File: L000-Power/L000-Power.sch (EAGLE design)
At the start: 20 parts

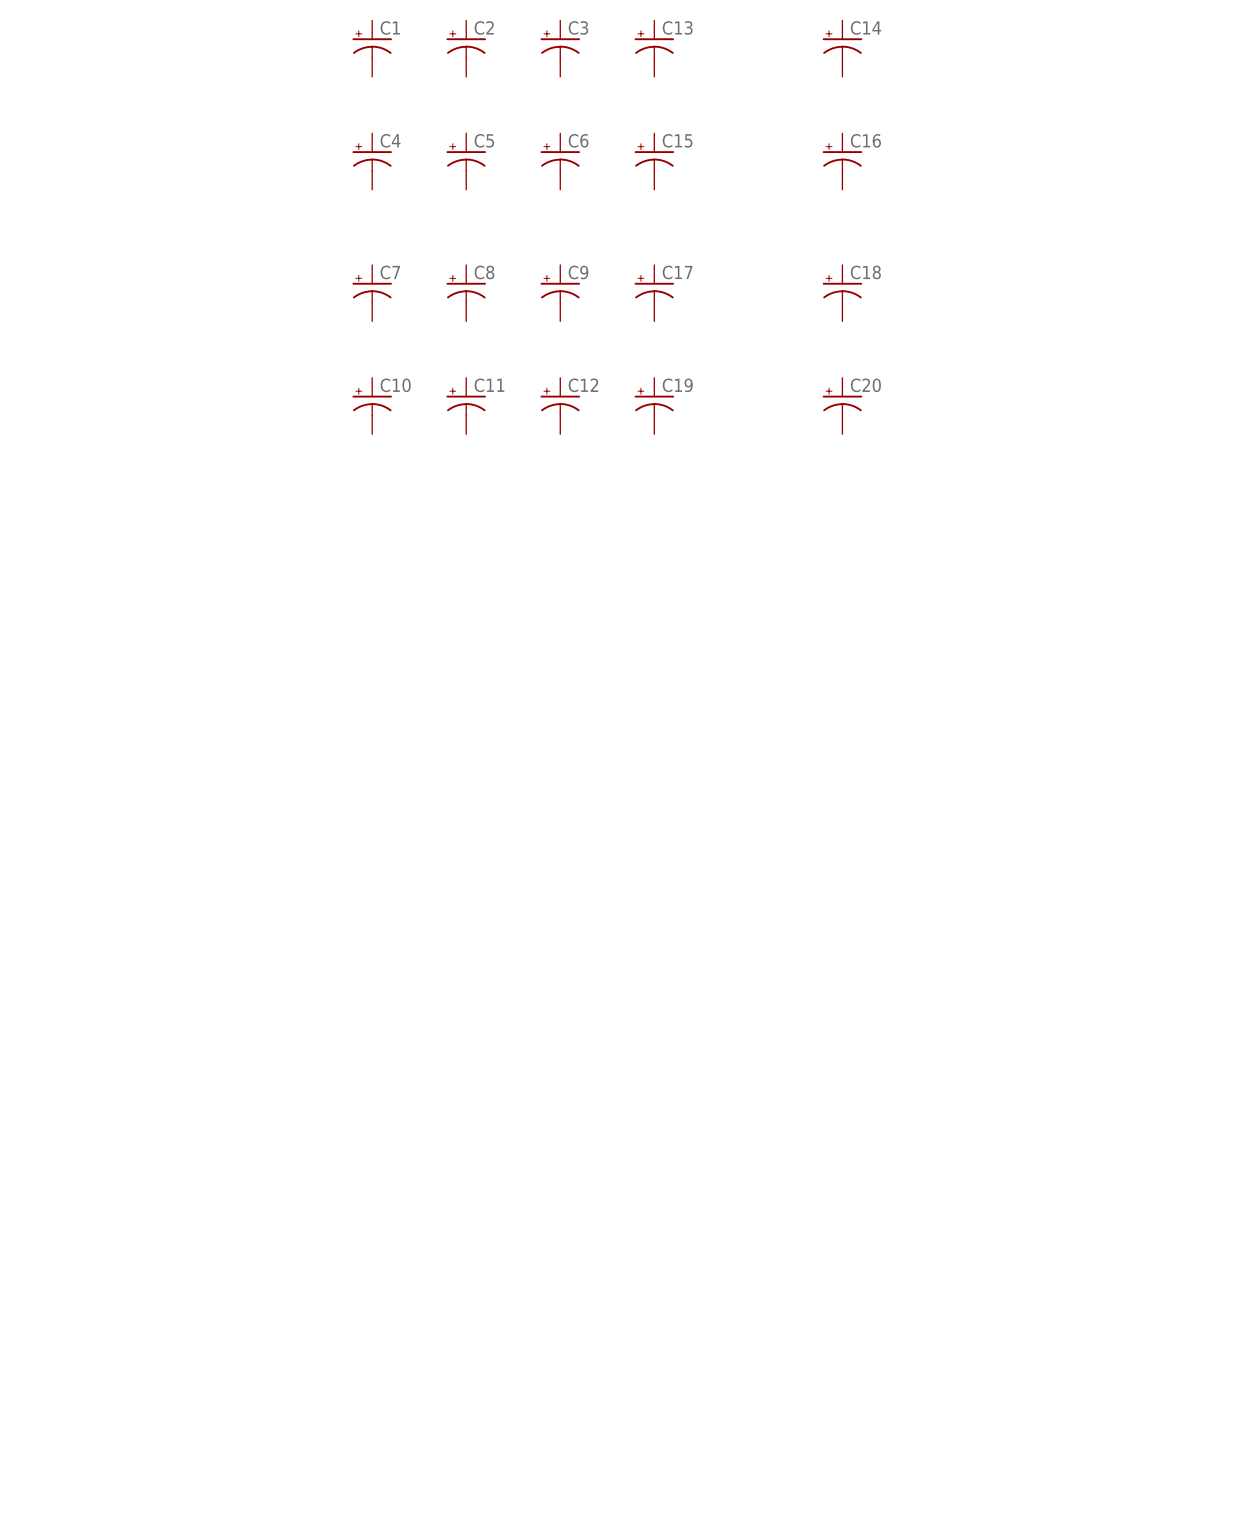
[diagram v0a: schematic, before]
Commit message: Add 9 and 5 volt dual supply circuits
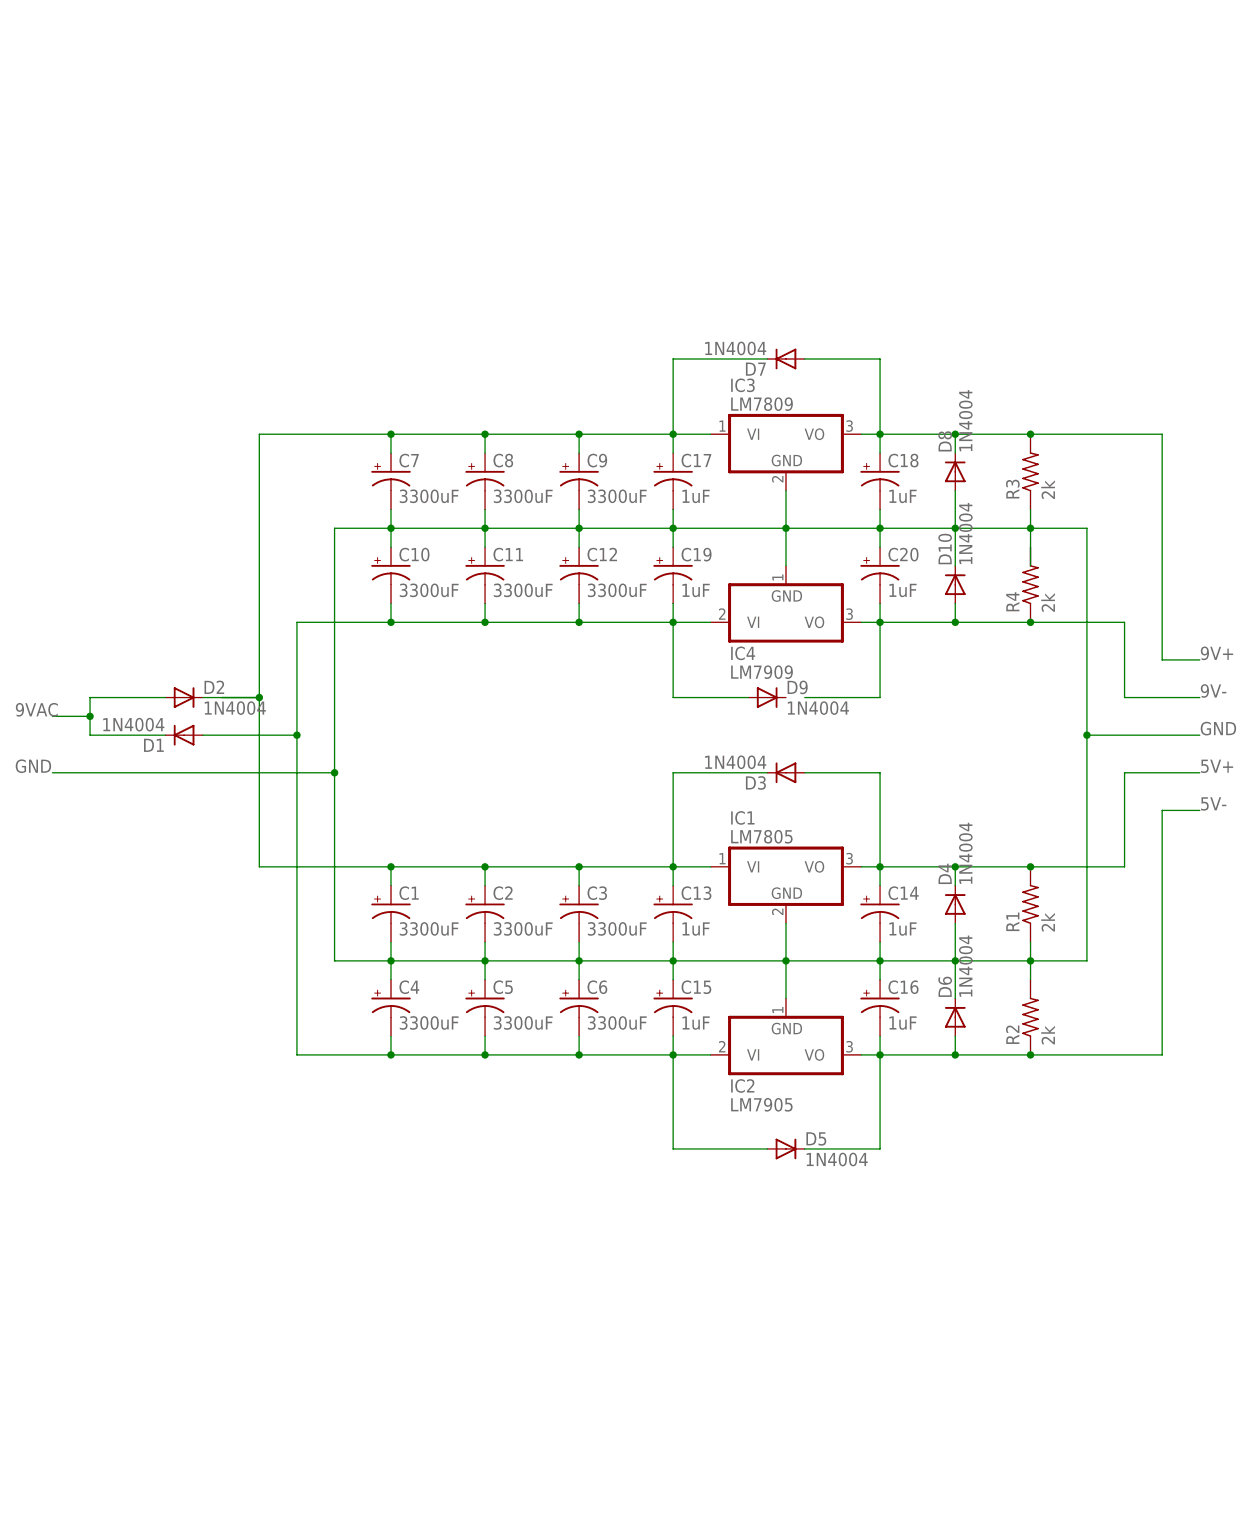
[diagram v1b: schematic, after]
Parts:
- added D1, D10, D2, D3, D4, D5, D6, D7, D8, D9: 1N4004, diode:1N4004
- added IC1: LM7805, linear:7805T
- added IC2: LM7905, linear:7905T
- added IC3: LM7809, linear:7808T
- added IC4: LM7909, linear:7908T
- added R1, R2, R3, R4: 2k, resistor:R-US_0309/10
- C1, C10, C11, C12, C2, C3, C4, C5, C6, C7, C8, C9: value (none) -> 3300uF
- C13, C14, C15, C16, C17, C18, C19, C20: value (none) -> 1uF
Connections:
- new net 5V+: C14.+, D3.A, D4.C, IC1.VO, R1.2
- new net 5V-: C16.-, D5.C, D6.A, IC2.VO, R2.1
- new net 9V+: C18.+, D7.A, D8.C, IC3.VO, R3.2
- new net 9V-: C20.-, D10.A, IC4.VO, R4.1
- new net 9VAC: D1.C, D2.A
- new net GND: C1.-, C10.+, C11.+, C12.+, C13.-, C14.-, C15.+, C16.+, C17.-, C18.-, C19.+, C2.-, C20.+, C3.-, C4.+, C5.+, C6.+, C7.-, C8.-, C9.-, D10.C, D4.A, D6.C, D8.A, IC1.GND, IC2.GND, IC3.GND, IC4.GND, R1.1, R2.2, R3.1
- new net N$1: C15.-, C4.-, C5.-, C6.-, D1.A, D5.A, IC2.VI
- new net N$7: C10.-, C11.-, C12.-, C19.-, D9.A, IC4.VI
- new net N$8: C1.+, C13.+, C17.+, C2.+, C3.+, C7.+, C8.+, C9.+, D2.C, D3.C, D7.C, IC1.VI, IC3.VI
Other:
- moved on the sheet: C1, C10, C11, C12, C13, C14, C15, C16, C17, C18, C19, C2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

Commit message: Fix errors
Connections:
- removed net N$7: C10.-, C11.-, C12.-, C19.-, D9.A, IC4.VI
- net 9V-: now also D9.C
- net GND: now also R4.2
- net N$1: now also C10.-, C11.-, C12.-, C19.-, D9.A, IC4.VI
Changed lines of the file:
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@@
 <wire x1="106.68" y1="-20.32" x2="106.68" y2="-22.86" width="0.1524" layer="91"/>
 <junction x="106.68" y="-22.86"/>
-<wire x1="106.68" y1="-22.86" x2="106.68" y2="-27.94" width="0.1524" layer="91"/>
 <wire x1="114.3" y1="-22.86" x2="114.3" y2="-50.8" width="0.1524" layer="91"/>
 <wire x1="114.3" y1="-50.8" x2="114.3" y2="-81.28" width="0.1524" layer="91"/>
@@
 <junction x="114.3" y="-50.8"/>
 <label x="129.54" y="-50.8" size="1.778" layer="95"/>
+<pinref part="R4" gate="G$1" pin="2"/>
+<wire x1="106.68" y1="-25.4" x2="106.68" y2="-22.86" width="0.1524" layer="91"/>
 </segment>
 </net>
@@
 </segment>
 </net>
-<net name="N$7" class="0">
-<segment>
-<wire x1="58.42" y1="-35.56" x2="45.72" y2="-35.56" width="0.1524" layer="91"/>
-<pinref part="C10" gate="G$1" pin="-"/>
-<wire x1="45.72" y1="-35.56" x2="33.02" y2="-35.56" width="0.1524" layer="91"/>
-<wire x1="33.02" y1="-35.56" x2="20.32" y2="-35.56" width="0.1524" layer="91"/>
-<wire x1="20.32" y1="-35.56" x2="12.7" y2="-35.56" width="0.1524" layer="91"/>
-<wire x1="20.32" y1="-33.02" x2="20.32" y2="-35.56" width="0.1524" layer="91"/>
-<junction x="20.32" y="-35.56"/>
-<pinref part="C11" gate="G$1" pin="-"/>
-<wire x1="33.02" y1="-33.02" x2="33.02" y2="-35.56" width="0.1524" layer="91"/>
-<junction x="33.02" y="-35.56"/>
-<pinref part="C12" gate="G$1" pin="-"/>
-<wire x1="45.72" y1="-33.02" x2="45.72" y2="-35.56" width="0.1524" layer="91"/>
-<junction x="45.72" y="-35.56"/>
-<pinref part="C19" gate="G$1" pin="-"/>
-<wire x1="58.42" y1="-33.02" x2="58.42" y2="-35.56" width="0.1524" layer="91"/>
-<pinref part="IC4" gate="A1" pin="VI"/>
-<wire x1="58.42" y1="-35.56" x2="63.5" y2="-35.56" width="0.1524" layer="91"/>
-<junction x="58.42" y="-35.56"/>
-<wire x1="58.42" y1="-35.56" x2="58.42" y2="-45.72" width="0.1524" layer="91"/>
-<pinref part="D9" gate="1" pin="A"/>
-<wire x1="68.58" y1="-45.72" x2="58.42" y2="-45.72" width="0.1524" layer="91"/>
-</segment>
-</net>
 <net name="9V+" class="0">
 <segment>
@@
 <wire x1="96.52" y1="-33.02" x2="96.52" y2="-35.56" width="0.1524" layer="91"/>
 <junction x="96.52" y="-35.56"/>
-<wire x1="76.2" y1="-45.72" x2="86.36" y2="-45.72" width="0.1524" layer="91"/>
-<wire x1="86.36" y1="-45.72" x2="86.36" y2="-35.56" width="0.1524" layer="91"/>
 <wire x1="119.38" y1="-35.56" x2="119.38" y2="-45.72" width="0.1524" layer="91"/>
 <wire x1="119.38" y1="-45.72" x2="129.54" y2="-45.72" width="0.1524" layer="91"/>
 <label x="129.54" y="-45.72" size="1.778" layer="95"/>
+<pinref part="D9" gate="1" pin="C"/>
+<wire x1="73.66" y1="-45.72" x2="86.36" y2="-45.72" width="0.1524" layer="91"/>
+<wire x1="86.36" y1="-45.72" x2="86.36" y2="-35.56" width="0.1524" layer="91"/>
 </segment>
 </net>
 <net name="N$1" class="0">
 <segment>
-<wire x1="12.7" y1="-35.56" x2="7.62" y2="-35.56" width="0.1524" layer="91"/>
-<wire x1="7.62" y1="-35.56" x2="7.62" y2="-50.8" width="0.1524" layer="91"/>
 <wire x1="7.62" y1="-50.8" x2="-5.08" y2="-50.8" width="0.1524" layer="91"/>
 <pinref part="IC2" gate="A1" pin="VI"/>
@@
 <wire x1="58.42" y1="-106.68" x2="71.12" y2="-106.68" width="0.1524" layer="91"/>
 <wire x1="7.62" y1="-50.8" x2="7.62" y2="-93.98" width="0.1524" layer="91"/>
+<pinref part="D1" gate="1" pin="A"/>
+<wire x1="7.62" y1="-50.8" x2="7.62" y2="-35.56" width="0.1524" layer="91"/>
 <junction x="7.62" y="-50.8"/>
-<pinref part="D1" gate="1" pin="A"/>
-</segment>
-</net>
+<wire x1="58.42" y1="-35.56" x2="45.72" y2="-35.56" width="0.1524" layer="91"/>
+<pinref part="C10" gate="G$1" pin="-"/>
+<wire x1="45.72" y1="-35.56" x2="33.02" y2="-35.56" width="0.1524" layer="91"/>
+<wire x1="33.02" y1="-35.56" x2="20.32" y2="-35.56" width="0.1524" layer="91"/>
+<wire x1="20.32" y1="-33.02" x2="20.32" y2="-35.56" width="0.1524" layer="91"/>
+<pinref part="C11" gate="G$1" pin="-"/>
+<wire x1="33.02" y1="-33.02" x2="33.02" y2="-35.56" width="0.1524" layer="91"/>
+<junction x="33.02" y="-35.56"/>
+<pinref part="C12" gate="G$1" pin="-"/>
+<wire x1="45.72" y1="-33.02" x2="45.72" y2="-35.56" width="0.1524" layer="91"/>
+<junction x="45.72" y="-35.56"/>
+<pinref part="C19" gate="G$1" pin="-"/>
+<wire x1="58.42" y1="-33.02" x2="58.42" y2="-35.56" width="0.1524" layer="91"/>
+<pinref part="IC4" gate="A1" pin="VI"/>
+<wire x1="58.42" y1="-35.56" x2="63.5" y2="-35.56" width="0.1524" layer="91"/>
+<junction x="58.42" y="-35.56"/>
+<wire x1="58.42" y1="-35.56" x2="58.42" y2="-45.72" width="0.1524" layer="91"/>
+<pinref part="D9" gate="1" pin="A"/>
+<wire x1="68.58" y1="-45.72" x2="58.42" y2="-45.72" width="0.1524" layer="91"/>
+<wire x1="7.62" y1="-35.56" x2="20.32" y2="-35.56" width="0.1524" layer="91"/>
+<junction x="20.32" y="-35.56"/>
+</segment>
+</net>

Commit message: Finished schematic
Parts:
- added X1: JST-XH-2PIN, SRG:JST-PH_2-PIN_HEADER
- added X10, X11, X12, X13, X14, X15, X16, X17, X18, X19, X2, X20, X21, X3, X4, X5, X6, X7, X8, X9: JST-XH-5PIN, SRG:JST-PH_5-PIN_HEADER
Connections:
- net 5V+: now also X12.2, X13.2, X14.2, X15.2, X16.2, X17.2, X18.2, X19.2, X20.2, X21.2
- net 5V-: now also X11.1, X12.1, X13.1, X14.1, X15.1, X16.1, X17.1, X18.1, X19.1, X20.1, X21.1
- net 9V+: now also X11.4, X12.4, X13.4, X14.4, X15.4, X16.4, X17.4, X18.4, X19.4, X20.4, X21.4
- net 9V-: now also X12.3, X13.3, X14.3, X15.3, X16.3, X17.3, X18.3, X19.3, X20.3, X21.3
- net 9VAC: now also X1.1
- net GND: now also X1.2, X12.5, X13.5, X14.5, X15.5, X16.5, X17.5, X18.5, X19.5, X20.5, X21.5
